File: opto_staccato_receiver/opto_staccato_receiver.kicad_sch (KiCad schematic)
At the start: 17 parts, among them J3 120/240VAC, J4 SCR out, J7 Jumper, J8 Jumper, Q4 IF D92, Q5 P30N06LE, Q6 2N3904, T2 FS28-200-C2, U5 LM7812_TO220

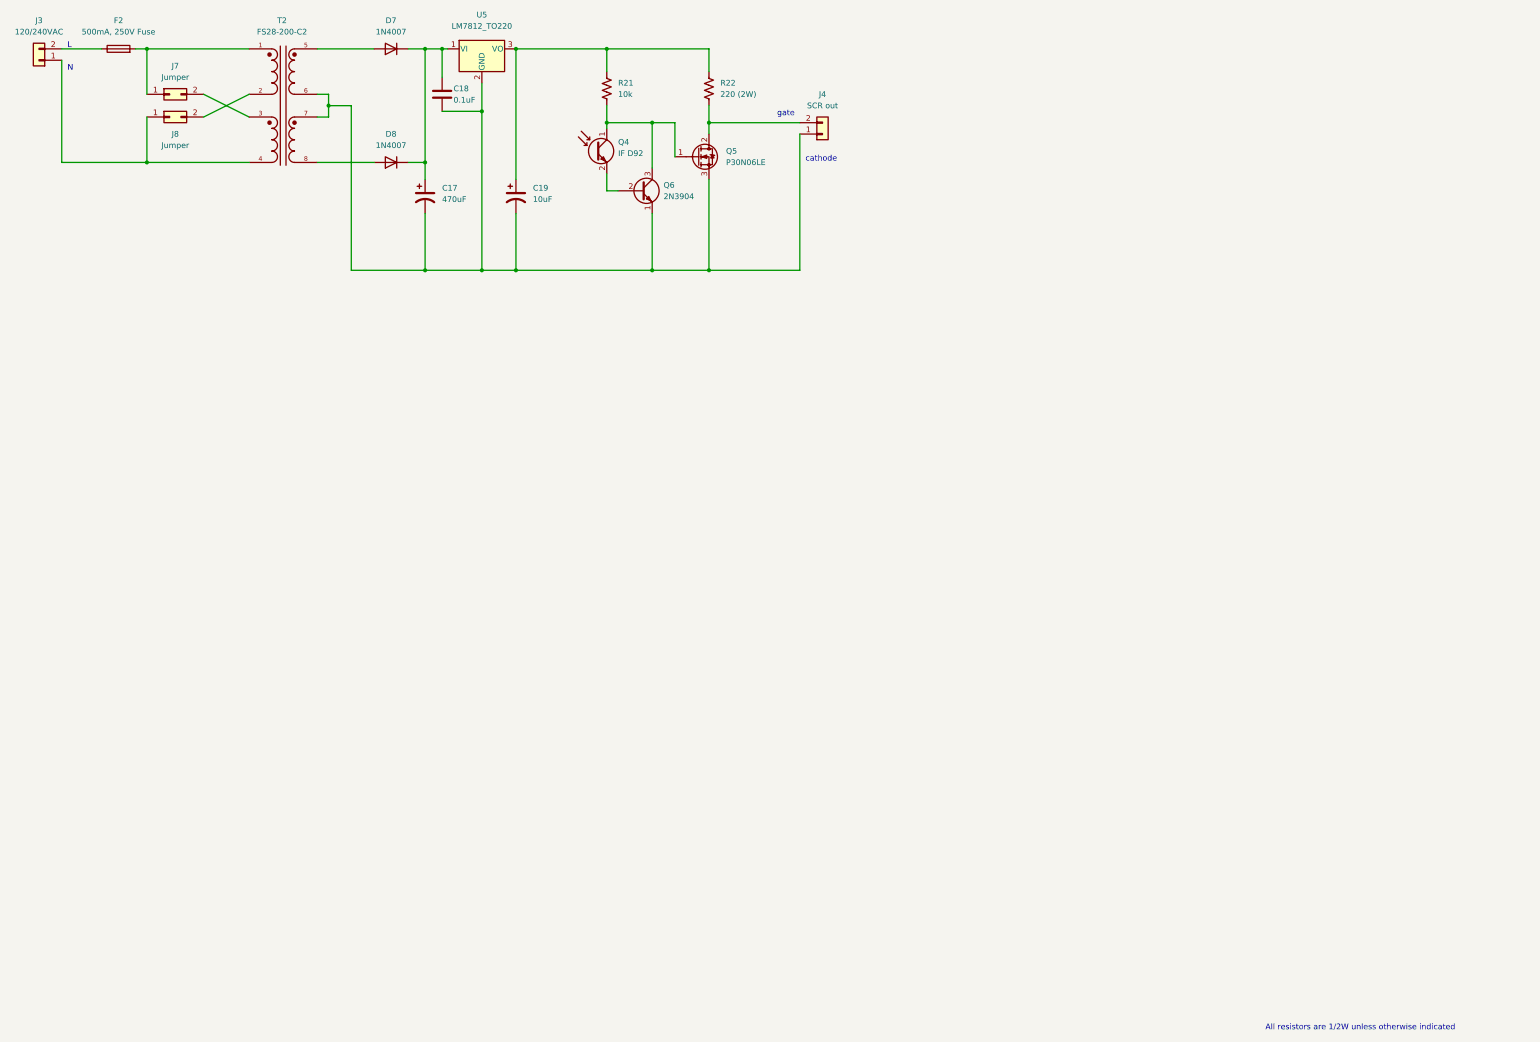
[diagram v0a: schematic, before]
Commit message: Add license to source files and images of schematics
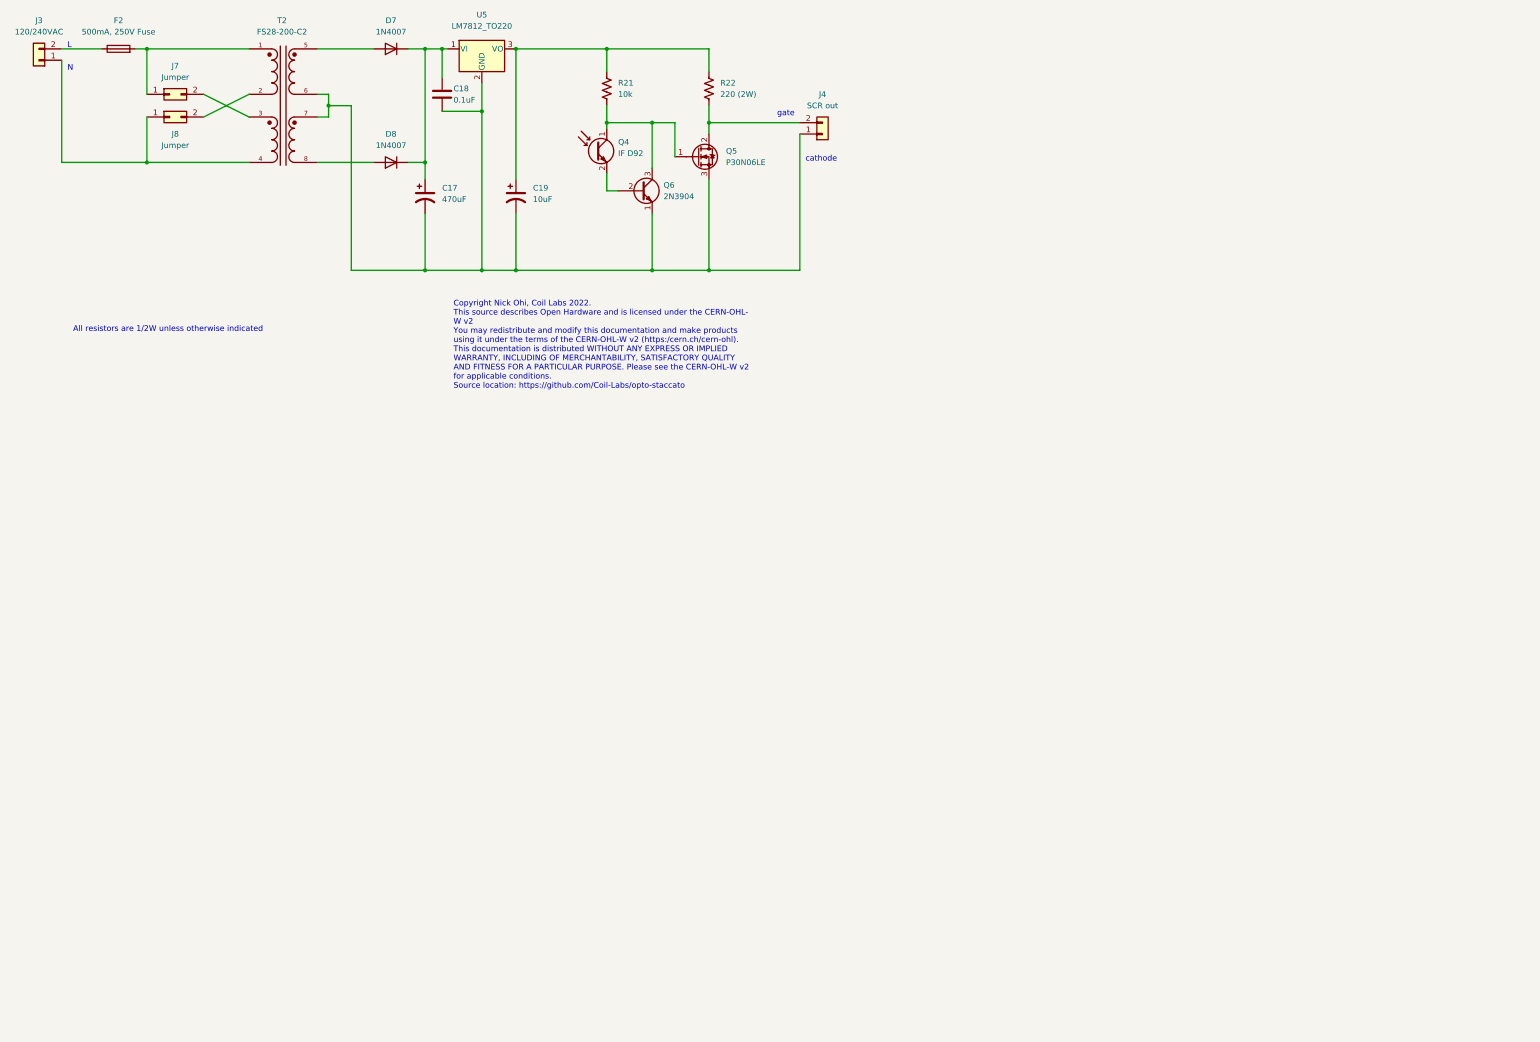
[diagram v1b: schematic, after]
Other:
- note added: "Copyright Nick Ohi, Coil Labs 2022. This source describes Open Hardware and is licensed under the CERN-OHL- W v2 You may redistribute and modify this documentation and make products using it under the terms of the CERN-OHL-W v2 (https:/cern.ch/cern-ohl). This documentation is distributed WITHOUT ANY EXPRESS OR IMPLIED WARRANTY, INCLUDING OF MERCHANTABILITY, SATISFACTORY QUALITY AND FITNESS FOR A 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"
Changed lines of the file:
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@@
 (kicad_sch (version 20211123) (generator eeschema)
-  (paper "A3")
+  (paper "A4")
   (junction (at 52.07 38.1) (diameter 0) (color 0 0 0 0)
   )
@@
     (effects (font (size 1.27 1.27)) (justify left bottom))
   )
-  (text "All resistors are 1/2W unless otherwise indicated" (at 302.26 257.81 0)
-    (effects (font (size 1.27 1.27)) (justify left bottom))
-  )
+  (text "All resistors are 1/2W unless otherwise indicated" (at 35.56 101.6 0)
+    (effects (font (size 1.27 1.27)) (justify left bottom))
+  )
+  (text "Copyright Nick Ohi, Coil Labs 2022.\nThis source describes Open Hardware and is licensed under the CERN-OHL-\nW v2\nYou may redistribute and modify this documentation and make products\nusing it under the terms of the CERN-OHL-W v2 (https:/cern.ch/cern-ohl).\nThis documentation is distributed WITHOUT ANY EXPRESS OR IMPLIED\nWARRANTY, INCLUDING OF MERCHANTABILITY, SATISFACTORY QUALITY\nAND FITNESS FOR A PARTICULAR PURPOSE. Please see the CERN-OHL-W v2\nfor applicable conditions.\nSource location: https://github.com/Coil-Labs/opto-staccato"
+    (at 120.65 114.3 0)
+    (effects (font (size 1.27 1.27)) (justify left bottom))
+  )
